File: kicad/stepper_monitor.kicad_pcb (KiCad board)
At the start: 2 copper layers, 39.5 x 54.5 mm, 63 parts, among them J1 Conn_01x04_Pin, J2 Conn_01x04_Pin, J3 Conn_01x02_Pin, J4 USB_C_Receptacle_USB2.0, J5 JTAG, Q1 MMDT2222A, SW1 SW_Push, U1 5V, U2 CP2102N-A01-GQFN28, U3 AMS1117-3.3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

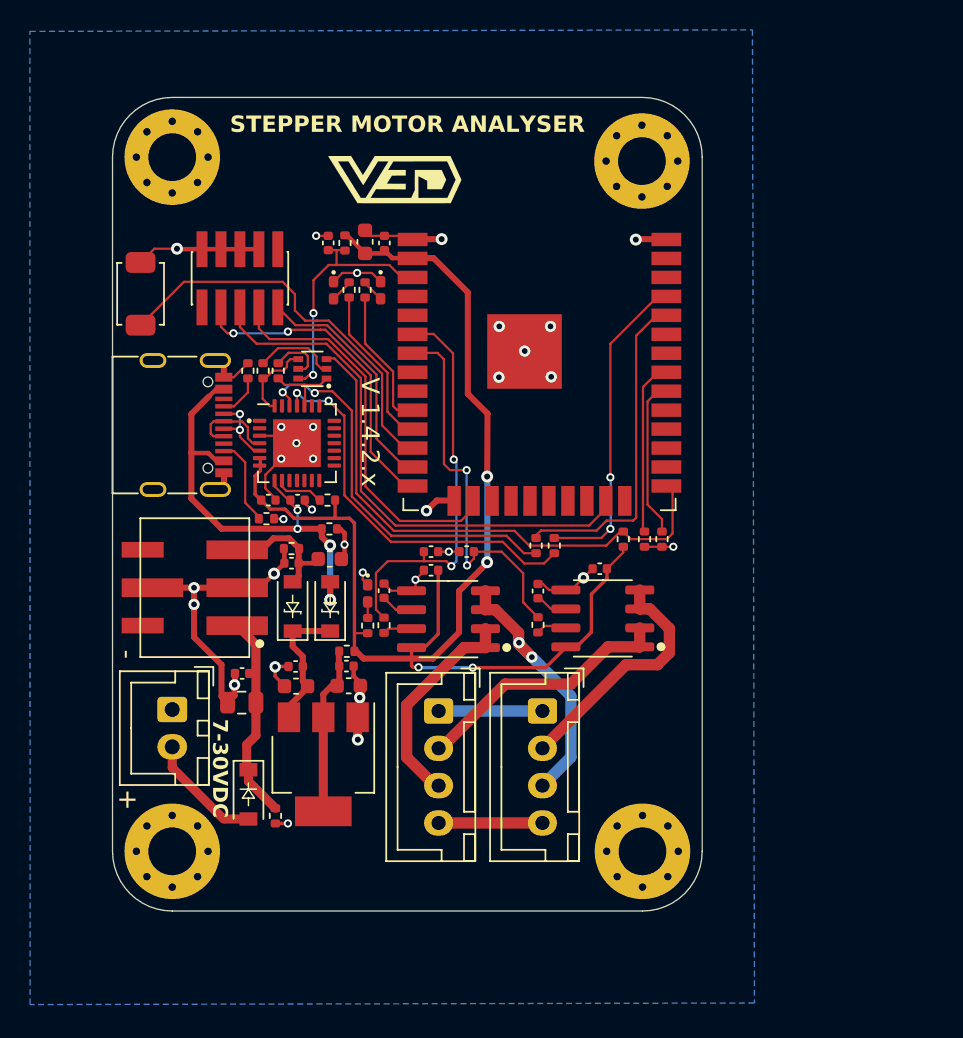
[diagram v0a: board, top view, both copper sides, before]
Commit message: New version without Mornsun regulator
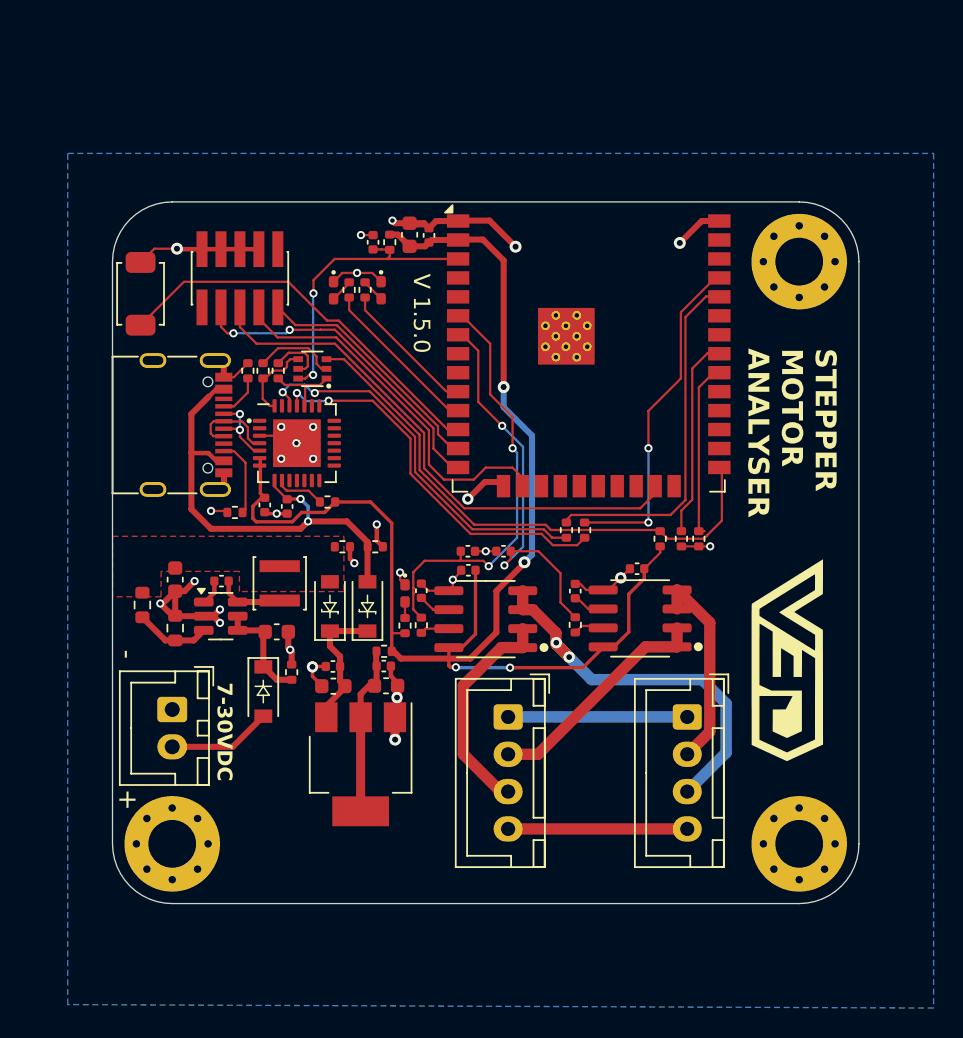
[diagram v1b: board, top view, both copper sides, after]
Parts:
- removed C5: 10u, Capacitor_SMD:C_0603_1608Metric
- removed H1: MountingHole, MountingHole:MountingHole_3.2mm_M3_Pad_Via
- removed U6: ESP32-WROOM-32U-N4, stepper_monitor:ESP32-WROOM-32U
- added L1: 18uH 580mA, Inductor_SMD:L_Sunlord_SWPA3012S, F.Cu at (11.2, -18.4)
- added R21: 88.7k, Resistor_SMD:R_0603_1608Metric, F.Cu at (2.00, -17.0)
- added R22: 22.1k, Resistor_SMD:R_0603_1608Metric, F.Cu at (4.20, -15.4)
- added U7: ESP32-WROOM-32E-R2, RF_Module:ESP32-WROOM-32D, F.Cu at (31.9, -34.5)
- C1: value 10u 50V -> 2.2uF 50V; footprint Capacitor_SMD:C_0805_2012Metric -> Capacitor_SMD:C_0603_1608Metric
- C2: value 100n 50V -> 100nF
- C3: value 100n -> 22uF; footprint Capacitor_SMD:C_0402_1005Metric -> Capacitor_SMD:C_0603_1608Metric
- D5, D6: value B5819W -> B5819W
- U1: value 5V -> TPS560430; footprint stepper_monitor:Converter_DCDC -> Package_TO_SOT_SMD:SOT-23-6
- moved H3 57.7 mm to (46.0, -40.0)
- moved H2 55.5 mm to (4.00, -1.00)
- moved G*** 41.6 mm to (45.2, -13.3), turned to -90 degrees
- moved H4 10.5 mm to (46.0, -1.00)
- moved J2 9.71 mm to (38.5, -9.50)
- moved R3 9.69 mm to (12.0, -12.5), turned to 90 degrees
- moved C3 7.87 mm to (4.20, -18.7), turned to -90 degrees
- moved D3 6.96 mm to (10.1, -11.2)
- moved C2 6.34 mm to (7.30, -18.6)
- moved C1 5.29 mm to (11.0, -15.2)
- moved J1 4.67 mm to (26.5, -9.50)
- moved R8 3.41 mm to (15.4, -20.9), turned to 180 degrees
- moved R9 3.30 mm to (17.6, -20.9)
- moved C13 3.03 mm to (21.2, -41.8)
- moved C12 3.02 mm to (19.9, -41.8)
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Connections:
- C1 pad 1: GNDD -> /VIN
- C1 pad 2: Net-(#FLG02-pwr) -> GND
- C10 pad 1: GNDD -> GND
- C11 pad 1: GNDD -> GND
- C12 pad 1: GNDD -> GND
- C13 pad 2: GNDD -> GND
- C14 pad 1: GNDD -> GND
- C15 pad 1: GNDD -> GND
- C16 pad 2: GNDD -> GND
- C17 pad 1: GNDD -> GND
- C18 pad 1: GNDD -> GND
- C19 pad 2: GNDD -> GND
- C2 pad 1: GNDD -> /CB
- C2 pad 2: Net-(#FLG02-pwr) -> /5V
- C3 pad 1: GNDD -> /Vout
- C3 pad 2: Net-(D6-A) -> GND
- C4 pad 1: GNDD -> GND
- C6 pad 1: GNDD -> GND
- C7 pad 2: GNDD -> GND
- C8 pad 1: GNDD -> GND
- C9 pad 1: GNDD -> GND
- D1 pad 1: GNDD -> GND
- D2 pad 1: GNDD -> GND
- D3 pad 1: Net-(#FLG02-pwr) -> /VIN
- D4 pad 1: GNDD -> GND
- D6 pad 2: Net-(D6-A) -> /Vout
- J3 pad 1: GNDD -> GND
- J4 pad G: GNDD -> GND
- J4 pad SHLD: GNDD -> GND
- J5 pad 3: GNDD -> GND
- J5 pad 5: GNDD -> GND
- J5 pad 7: GNDD -> GND
- J5 pad 9: GNDD -> GND
- R17 pad 2: GNDD -> GND
- R18 pad 2: GNDD -> GND
- R3 pad 1: Net-(#FLG02-pwr) -> /VIN
- R3 pad 2: GNDD -> GND
- R4 pad 1: GNDD -> GND
- R5 pad 1: GNDD -> GND
- R8 pad 1: GNDD -> GND
- R8 pad 2: Net-(D6-A) -> /Vout
- R9 pad 1: GNDD -> GND
- SW1 pad 1: GNDD -> GND
- U1 pad 1: Net-(#FLG02-pwr) -> /CB
- U1 pad 2: GNDD -> GND
- U1 pad 3: Net-(D6-A) -> /FB
- U1 pad 4: unconnected-(U1-Pad4) -> /VIN
- U1 pad 5: GNDD -> /VIN
- U1 pad 6: unconnected-(U1-Pad6) -> /5V
- U2 pad 29: GNDD -> GND
- U2 pad 3: GNDD -> GND
- U3 pad 1: GNDD -> GND
- U4 pad 5: GNDD -> GND
- U5 pad 5: GNDD -> GND
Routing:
- net GNDD: track 79.9 -> 0.00 mm, vias 32 -> 0
- net GND: track 0.00 -> 73.9 mm, vias 0 -> 29
- net Net-(#FLG02-pwr): track 13.8 -> 0.00 mm
- net Net-(D6-A): track 8.58 -> 0.00 mm
- net Net-(J2-Pin_3): track 17.9 -> 26.2 mm
- net /VIN: track 0.00 -> 7.45 mm
- net +3V3: track 89.8 -> 95.2 mm
- net Net-(J1-Pin_4): track 6.96 -> 12.0 mm
- net Net-(J1-Pin_1): track 6.96 -> 12.0 mm
- net /FB: track 0.00 -> 5.03 mm
- net /5V: track 0.00 -> 4.51 mm
- net Net-(J2-Pin_2): track 16.6 -> 13.8 mm
- net EN: track 17.8 -> 19.6 mm
- net /CB: track 0.00 -> 1.74 mm
- net CFG2: track 11.7 -> 13.3 mm
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- added copper zone on F.Cu, net /Vout
- added copper zone on B.Cu, net GND
- removed copper zone on B.Cu, net GNDD
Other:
- board size 39.5 x 54.5 mm -> 50 x 47 mm
- board text added: "V 1.5.0"
- board text removed: "JLCJLCJLCJLC"
- board text removed: "V 1.4.2.x"
